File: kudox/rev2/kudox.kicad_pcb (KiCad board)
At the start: 2 copper layers, 144.9 x 130.2 mm, 83 parts, among them K0 KEYSW, K1 KEYSW, K10 KEYSW, K11 KEYSW, K12 KEYSW, K13 KEYSW, K14 KEYSW, K15 KEYSW, K16 KEYSW, K2 KEYSW, K20 KEYSW, K21 KEYSW, K22 KEYSW, K23 KEYSW, K24 KEYSW, K25 KEYSW, K3 KEYSW, K30 KEYSW, K31 KEYSW, K32 KEYSW, K33 KEYSW, K34 KEYSW, K35 KEYSW, K4 KEYSW, K40 KEYSW, K41 KEYSW, K42 KEYSW, K43 KEYSW, K44 KEYSW, K45 KEYSW, K46 KEYSW, K5 KEYSW, K6 KEYSW, U1 ProMicro

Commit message: Add icons.
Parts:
- added G***: LOGO, kudox_footprints:kumao-icon-right-s, F.Cu at (214.4, 79.5)
- added G***: LOGO, kudox_footprints:kumao-icon-left-s, B.Cu at (212.5, 79.5)
- moved -3 59.6 mm to (186.5, 127.6)
- moved REF*** 59.6 mm to (186.5, 127.5)
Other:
- board text added: "Kumao Kobo"
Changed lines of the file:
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@@
   (general
     (thickness 1.6)
-    (drawings 144)
+    (drawings 146)
     (tracks 1073)
     (zones 0)
-    (modules 83)
+    (modules 85)
     (nets 56)
   )
@@
     (add_net row4)
   )
+  (module kudox_footprints:kumao-icon-right-s (layer F.Cu)
+    (at 214.36 79.46)
+    (fp_text reference G*** (at 0 0) (layer F.SilkS) hide
+      (effects (font (size 1.524 1.524) (thickness 0.3)))
+    )
+    (fp_text value LOGO (at 0.75 0) (layer F.SilkS) hide
+      (effects (font (size 1.524 1.524) (thickness 0.3)))
+    )
+    (fp_poly (pts (xy -0.930868 -5.159486) (xy -1.14711 -5.011628) (xy -1.272661 -4.792217) (xy -1.282073 -4.753185)
+      (xy -1.372829 -4.565927) (xy -1.55851 -4.366565) (xy -1.59531 -4.335942) (xy -1.819031 -4.170358)
+      (xy -2.118149 -3.967855) (xy -2.450838 -3.75494) (xy -2.775272 -3.558125) (xy -3.049626 -3.403917)
+      (xy -3.131736 -3.362156) (xy -3.34652 -3.244559) (xy -3.627191 -3.072548) (xy -3.941813 -2.867742)
+      (xy -4.258447 -2.651762) (xy -4.545156 -2.446227) (xy -4.770003 -2.272756) (xy -4.869631 -2.185724)
+      (xy -5.29031 -1.748766) (xy -5.642089 -1.306576) (xy -5.962716 -0.809046) (xy -6.12731 -0.516173)
+      (xy -6.415251 0.078823) (xy -6.651288 0.69423) (xy -6.829649 1.305692) (xy -6.944561 1.88885)
+      (xy -6.990251 2.419348) (xy -6.960948 2.872827) (xy -6.947343 2.944024) (xy -6.904714 3.239028)
+      (xy -6.923194 3.496745) (xy -6.949219 3.613468) (xy -6.997247 3.939391) (xy -6.947292 4.186779)
+      (xy -6.791627 4.365563) (xy -6.522525 4.485675) (xy -6.22393 4.545709) (xy -5.855923 4.599816)
+      (xy -5.36786 4.677596) (xy -4.756544 4.779578) (xy -4.01878 4.906288) (xy -3.606347 4.97823)
+      (xy -3.079792 5.061525) (xy -2.606696 5.113696) (xy -2.122474 5.140262) (xy -1.633311 5.146842)
+      (xy -1.242555 5.145736) (xy -0.960502 5.140227) (xy -0.762174 5.127029) (xy -0.622593 5.102856)
+      (xy -0.516783 5.064422) (xy -0.419766 5.00844) (xy -0.380136 4.981969) (xy -0.096594 4.723435)
+      (xy 0.082966 4.414125) (xy 0.143527 4.08998) (xy 0.092454 3.837187) (xy -0.055565 3.674124)
+      (xy -0.292725 3.608857) (xy -0.32253 3.608006) (xy -0.487055 3.579514) (xy -0.699317 3.509708)
+      (xy -0.778068 3.476463) (xy -1.041266 3.28886) (xy -1.205514 3.018229) (xy -1.260157 2.693501)
+      (xy -1.20787 2.429363) (xy -1.06478 2.118645) (xy -0.851542 1.788582) (xy -0.588812 1.466407)
+      (xy -0.297245 1.179355) (xy 0.002503 0.95466) (xy 0.101872 0.897694) (xy 0.468608 0.705683)
+      (xy 1.018972 0.993813) (xy 1.542609 1.219627) (xy 2.015432 1.322004) (xy 2.437966 1.300939)
+      (xy 2.810737 1.156428) (xy 3.048321 0.976216) (xy 3.189112 0.829127) (xy 3.259189 0.69584)
+      (xy 3.282279 0.517555) (xy 3.28362 0.39316) (xy 3.252859 0.084526) (xy 3.166646 -0.104325)
+      (xy 2.965804 -0.305936) (xy 2.693977 -0.530578) (xy 2.399686 -0.741751) (xy 2.131455 -0.902951)
+      (xy 2.057488 -0.938712) (xy 1.813434 -1.073147) (xy 1.57572 -1.244389) (xy 1.516507 -1.296529)
+      (xy 1.333052 -1.517412) (xy 1.279971 -1.714637) (xy 1.357161 -1.893663) (xy 1.503023 -2.021)
+      (xy 1.940441 -2.333816) (xy 2.260859 -2.602739) (xy 2.470164 -2.836516) (xy 2.574238 -3.043895)
+      (xy 2.578966 -3.233624) (xy 2.490233 -3.414449) (xy 2.463316 -3.448495) (xy 2.338917 -3.625616)
+      (xy 2.253717 -3.796567) (xy 2.249275 -3.81) (xy 2.115491 -4.073206) (xy 1.892659 -4.337957)
+      (xy 1.618533 -4.563455) (xy 1.472321 -4.649604) (xy 1.249251 -4.743576) (xy 0.940075 -4.848754)
+      (xy 0.580233 -4.955737) (xy 0.205168 -5.055122) (xy -0.149678 -5.137508) (xy -0.448865 -5.193493)
+      (xy -0.654081 -5.213684) (xy -0.930868 -5.159486)) (layer F.SilkS) (width 0.01))
+  )
+  (module kudox_footprints:kumao-icon-left-s (layer B.Cu)
+    (at 212.5 79.46 180)
+    (fp_text reference G*** (at 0 0 180) (layer F.SilkS) hide
+      (effects (font (size 1.524 1.524) (thickness 0.3)))
+    )
+    (fp_text value LOGO (at 0.75 0 180) (layer F.SilkS) hide
+      (effects (font (size 1.524 1.524) (thickness 0.3)))
+    )
+    (fp_poly (pts (xy -0.930868 5.159486) (xy -0.714626 5.011628) (xy -0.589075 4.792217) (xy -0.579663 4.753185)
+      (xy -0.488907 4.565927) (xy -0.303226 4.366565) (xy -0.266426 4.335942) (xy -0.042705 4.170358)
+      (xy 0.256413 3.967855) (xy 0.589102 3.75494) (xy 0.913536 3.558125) (xy 1.18789 3.403917)
+      (xy 1.27 3.362156) (xy 1.484784 3.244559) (xy 1.765455 3.072548) (xy 2.080077 2.867742)
+      (xy 2.396711 2.651762) (xy 2.68342 2.446227) (xy 2.908267 2.272756) (xy 3.007895 2.185724)
+      (xy 3.428574 1.748766) (xy 3.780353 1.306576) (xy 4.10098 0.809046) (xy 4.265574 0.516173)
+      (xy 4.553515 -0.078823) (xy 4.789552 -0.69423) (xy 4.967913 -1.305692) (xy 5.082825 -1.88885)
+      (xy 5.128515 -2.419348) (xy 5.099212 -2.872827) (xy 5.085607 -2.944024) (xy 5.042978 -3.239028)
+      (xy 5.061458 -3.496745) (xy 5.087483 -3.613468) (xy 5.135511 -3.939391) (xy 5.085556 -4.186779)
+      (xy 4.929891 -4.365563) (xy 4.660789 -4.485675) (xy 4.362194 -4.545709) (xy 3.994187 -4.599816)
+      (xy 3.506124 -4.677596) (xy 2.894808 -4.779578) (xy 2.157044 -4.906288) (xy 1.744611 -4.97823)
+      (xy 1.218056 -5.061525) (xy 0.74496 -5.113696) (xy 0.260738 -5.140262) (xy -0.228425 -5.146842)
+      (xy -0.619181 -5.145736) (xy -0.901234 -5.140227) (xy -1.099562 -5.127029) (xy -1.239143 -5.102856)
+      (xy -1.344953 -5.064422) (xy -1.44197 -5.00844) (xy -1.4816 -4.981969) (xy -1.765142 -4.723435)
+      (xy -1.944702 -4.414125) (xy -2.005263 -4.08998) (xy -1.95419 -3.837187) (xy -1.806171 -3.674124)
+      (xy -1.569011 -3.608857) (xy -1.539206 -3.608006) (xy -1.374681 -3.579514) (xy -1.162419 -3.509708)
+      (xy -1.083668 -3.476463) (xy -0.82047 -3.28886) (xy -0.656222 -3.018229) (xy -0.601579 -2.693501)
+      (xy -0.653866 -2.429363) (xy -0.796956 -2.118645) (xy -1.010194 -1.788582) (xy -1.272924 -1.466407)
+      (xy -1.564491 -1.179355) (xy -1.864239 -0.95466) (xy -1.963608 -0.897694) (xy -2.330344 -0.705683)
+      (xy -2.880708 -0.993813) (xy -3.404345 -1.219627) (xy -3.877168 -1.322004) (xy -4.299702 -1.300939)
+      (xy -4.672473 -1.156428) (xy -4.910057 -0.976216) (xy -5.050848 -0.829127) (xy -5.120925 -0.69584)
+      (xy -5.144015 -0.517555) (xy -5.145356 -0.39316) (xy -5.114595 -0.084526) (xy -5.028382 0.104325)
+      (xy -4.82754 0.305936) (xy -4.555713 0.530578) (xy -4.261422 0.741751) (xy -3.993191 0.902951)
+      (xy -3.919224 0.938712) (xy -3.67517 1.073147) (xy -3.437456 1.244389) (xy -3.378243 1.296529)
+      (xy -3.194788 1.517412) (xy -3.141707 1.714637) (xy -3.218897 1.893663) (xy -3.364759 2.021)
+      (xy -3.802177 2.333816) (xy -4.122595 2.602739) (xy -4.3319 2.836516) (xy -4.435974 3.043895)
+      (xy -4.440702 3.233624) (xy -4.351969 3.414449) (xy -4.325052 3.448495) (xy -4.200653 3.625616)
+      (xy -4.115453 3.796567) (xy -4.111011 3.81) (xy -3.977227 4.073206) (xy -3.754395 4.337957)
+      (xy -3.480269 4.563455) (xy -3.334057 4.649604) (xy -3.110987 4.743576) (xy -2.801811 4.848754)
+      (xy -2.441969 4.955737) (xy -2.066904 5.055122) (xy -1.712058 5.137508) (xy -1.412871 5.193493)
+      (xy -1.207655 5.213684) (xy -0.930868 5.159486)) (layer B.SilkS) (width 0.01))
+  )
   (module kudox_footprints:Mx_hotswappable (layer F.Cu)
     (at 211.03 147.72 330)
@@
   )
   (module Symbols:OSHW-Symbol_8.9x8mm_SilkScreen (layer B.Cu)
-    (at 213 74.16 180)
+    (at 186.53 127.55 180)
     (descr "Open Source Hardware Symbol")
     (tags "Logo Symbol OSHW")
@@
   )
   (module Symbols:OSHW-Symbol_8.9x8mm_SilkScreen (layer F.Cu)
-    (at 213 74.16)
+    (at 186.5 127.56)
     (descr "Open Source Hardware Symbol")
     (tags "Logo Symbol OSHW")
@@
       (net 2 row0) (solder_mask_margin -999))
   )
+  (gr_text "Kumao Kobo" (at 212 86.56) (layer B.SilkS)
+    (effects (font (size 1.2 1.2) (thickness 0.12)) (justify mirror))
+  )
+  (gr_text "Kumao Kobo" (at 212 86.56) (layer F.SilkS)
+    (effects (font (size 1.2 1.2) (thickness 0.12)))
+  )
   (dimension 130.2 (width 0.15) (layer Dwgs.User)

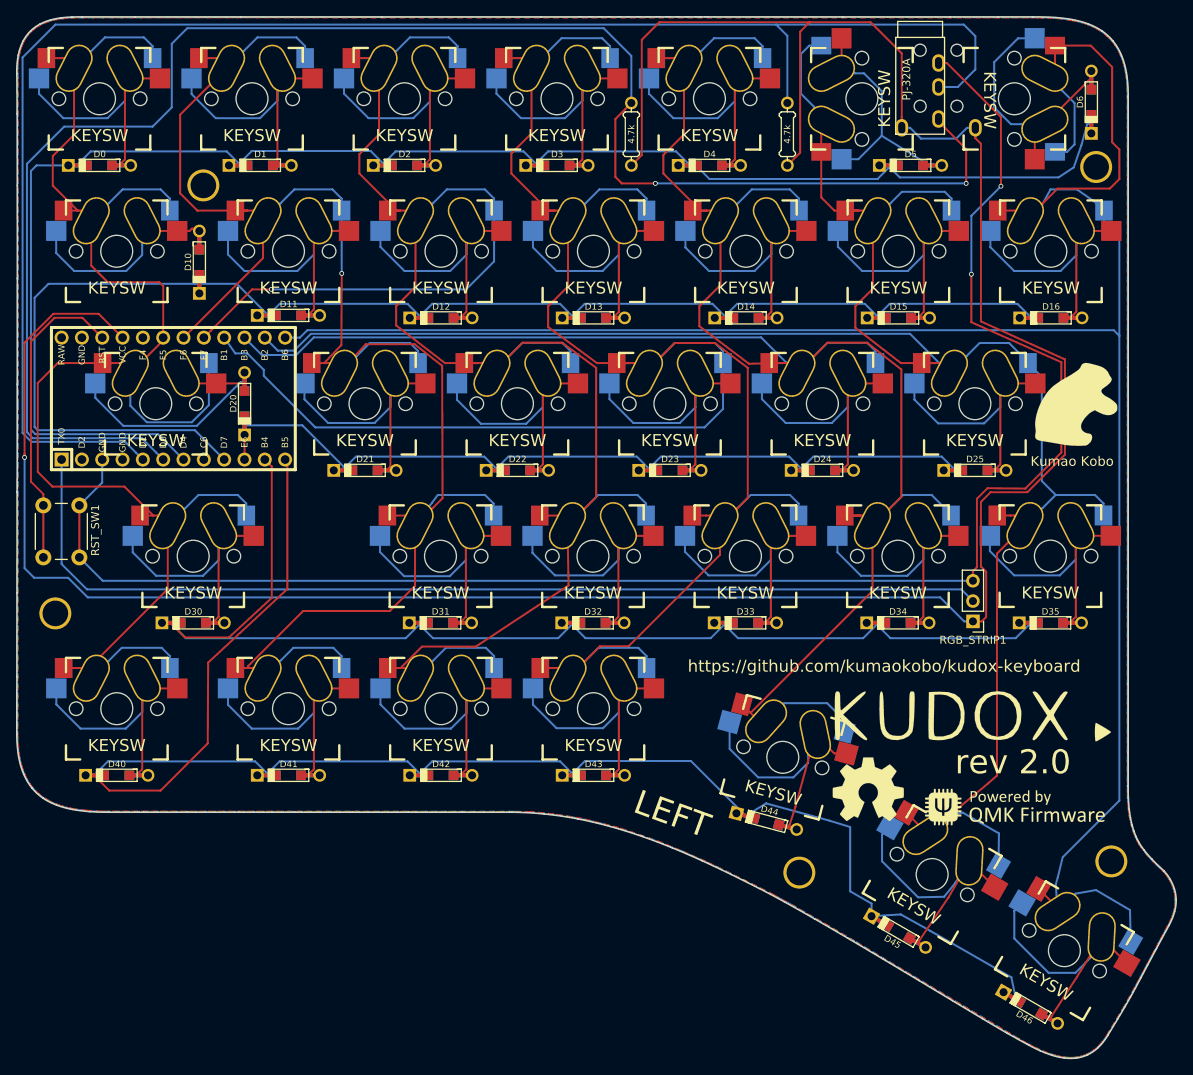
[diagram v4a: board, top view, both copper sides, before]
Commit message: Modified position of ProMicro.
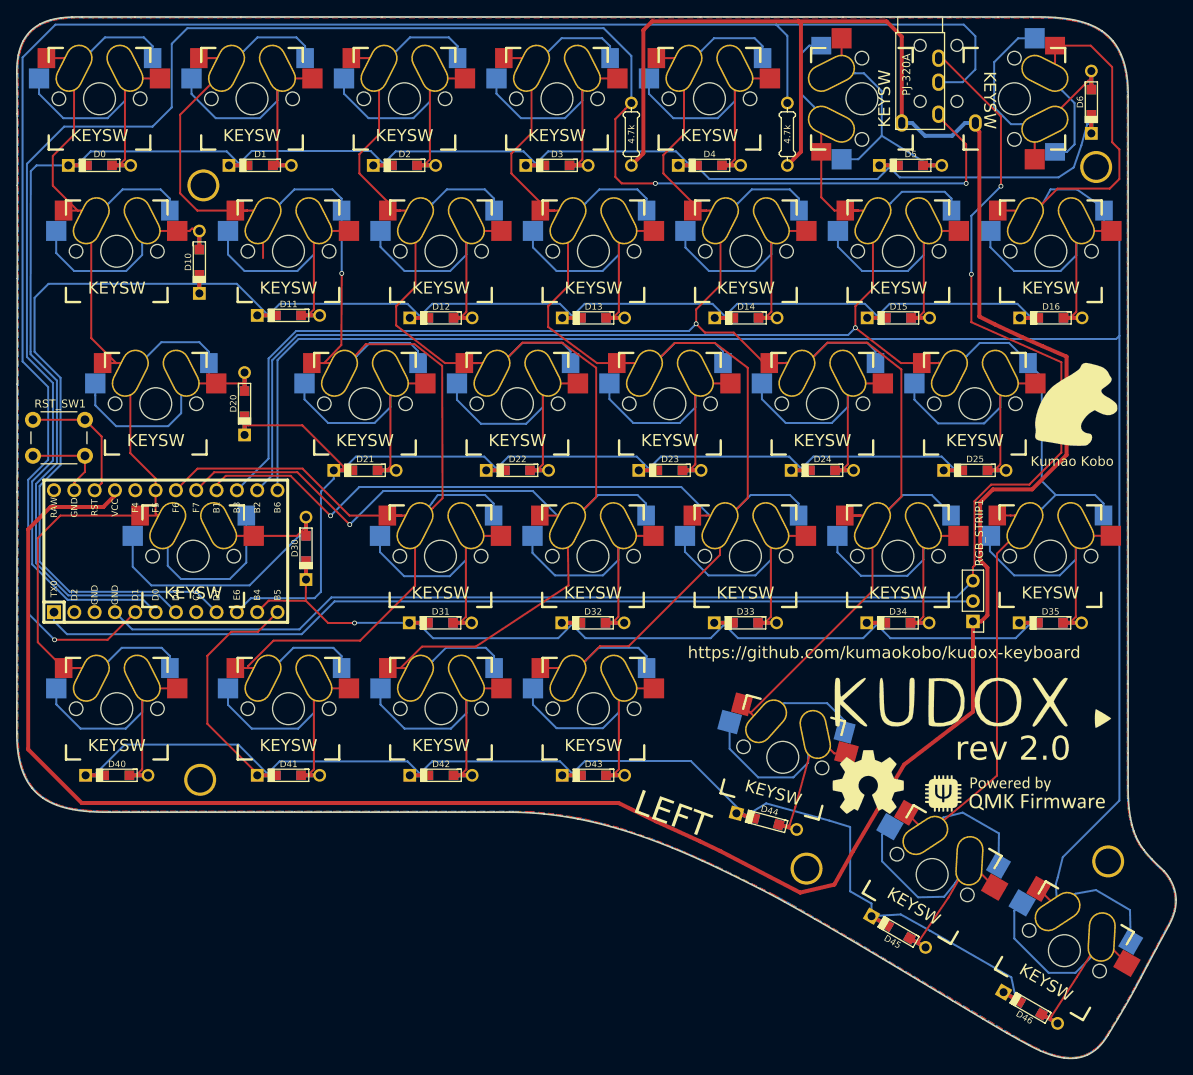
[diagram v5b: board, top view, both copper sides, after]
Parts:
- moved HOLE_M3 27.6 mm to (103.0, 126.4)
- moved U1 19.1 mm to (98.7, 97.8)
- moved RST_SW1 17.2 mm to (82.1, 81.4), turned to 0 degrees
- moved D30 16.9 mm to (116.2, 97.4), turned to 270 degrees
- moved G*** 1.70 mm to (205.1, 128.2)
- moved G*** 1.70 mm to (199.6, 116.7)
- moved G*** 1.70 mm to (198.7, 116.8)
- moved G*** 1.70 mm to (204.9, 128.1)
- moved HOLE_M3 1.03 mm to (178.8, 137.5)
- moved -3 0.90 mm to (186.5, 126.7)
- moved REF*** 0.90 mm to (186.5, 126.7)
- moved TRRS1 0.60 mm to (195.3, 33.0)
- moved HOLE_M3 0.40 mm to (216.5, 136.6)
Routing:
- net row3: track 160.8 -> 117.4 mm, vias 0 -> 1
- net row4: track 206.3 -> 180.3 mm
- net SDA: track 204.8 -> 229.7 mm, vias 0 -> 1
- net row2: track 109.3 -> 133.6 mm
- net VCC: track 331.8 -> 355.7 mm, vias 1 -> 0
- net RST: track 38.8 -> 16.5 mm
- net SCL: track 211.0 -> 230.3 mm
- net row1: track 188.1 -> 206.7 mm
- net row0: track 210.6 -> 229.1 mm
- net col6: track 285.5 -> 303.3 mm
- net col1: track 222.9 -> 240.6 mm
- net rgb_data: track 128.9 -> 118.4 mm
- net col0: track 202.9 -> 193.6 mm
- net col2: track 249.2 -> 256.3 mm
- net col3: track 274.3 -> 269.6 mm, vias 0 -> 1
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
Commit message: Flip K30.
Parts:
- moved R1 19.5 mm to (156.9, 45.7)
- moved R2 19.5 mm to (176.4, 45.7)
- moved U1 1.26 mm to (98.7, 99.0)
- moved D30 1.03 mm to (116.2, 98.5)
- moved RST_SW1 0.50 mm to (82.1, 81.9)
- turned K30 to 180 degrees
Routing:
- net row0: track 229.1 -> 275.4 mm, vias 0 -> 1
- net SCL: track 230.3 -> 256.9 mm, vias 2 -> 1
- net row1: track 206.7 -> 222.5 mm
- net Net-(D30-Pad2): track 41.0 -> 33.3 mm, vias 0 -> 1
- net GND: track 207.1 -> 208.8 mm
- net RST: track 16.5 -> 18.0 mm
- net col6: track 303.3 -> 304.6 mm
- net col4: track 277.1 -> 278.4 mm
- net col5: track 280.9 -> 282.2 mm
- net row4: track 180.3 -> 181.5 mm
- net col1: track 240.6 -> 241.6 mm
- net col2: track 256.3 -> 257.2 mm
- net row2: track 133.6 -> 134.4 mm
- net col3: track 269.6 -> 270.1 mm
- net row3: track 117.4 -> 116.9 mm
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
